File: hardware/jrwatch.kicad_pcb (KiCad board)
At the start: 4 copper layers, 36 x 36 mm, 47 parts, among them J1 TYPE-C-31-M-12, J2 FH12A-10S-0.5SH, J3 SM02B-SRSS-TB, J4 TC2030-IDC-NL, SW1 PWR/SHIP, SW2 USER, U1 MDBT50Q-1MV2, U2 nPM1300-QEAA-R7, U3 BMI270, U4 USBLC6-2SC6, Y1 32.768kHz

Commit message: Critical-net routing clean: USB pair, buck loops, crystal, VBUS entry, pours
Hand-constrained routes verified to zero DRC conflicts before autorouting.
Debug trail: QFN top row numbers right-to-left after flip, rot-90 passives
put pad1 south, USB-C A/B pads land mirrored — every hardcoded coordinate
re-derived from measured pad positions. One deliberate F.Cu crossover for
the interleaved USB pair; long USB run rides the empty top layer. USB skew
7.0mm = 46ps, 0.06% of a FS bit — documented, no serpentine.
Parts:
- moved R1 23.5 mm to (110.0, 101.5)
- moved R2 22.4 mm to (110.0, 103.2)
- moved C15 13.7 mm to (93.2, 98.6), turned to 180 degrees
- moved C4 11.3 mm to (84.7, 107.0)
- turned C16 to -90 degrees
- turned C17 to -90 degrees
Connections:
- U4 pad 1: USB_DP_CONN -> USB_DM_CONN
- U4 pad 3: USB_DM_CONN -> USB_DP_CONN
- U4 pad 4: USB_DM -> USB_DP
- U4 pad 6: USB_DP -> USB_DM
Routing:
- net 3V0: track 0.00 -> 19.9 mm, vias 0 -> 6
- net USB_DP_CONN: track 0.00 -> 17.1 mm
- net USB_DM_CONN: track 0.00 -> 16.8 mm, vias 0 -> 2
- net USB_DP: track 0.00 -> 16.1 mm, vias 0 -> 2
- net USB_DM: track 0.00 -> 13.0 mm, vias 0 -> 2
- net GND: track 0.00 -> 7.51 mm, vias 0 -> 8
- net N$3: track 0.00 -> 6.16 mm
- net 1V8_AUX: track 0.00 -> 5.20 mm
- net XL1: track 0.00 -> 5.08 mm
- net XL2: track 0.00 -> 4.57 mm
- net N$1: track 0.00 -> 4.57 mm
- net VBUS_USB: track 0.00 -> 1.72 mm, vias 0 -> 1
- added copper zone on In1.Cu, net 3V0
- added copper zone on B.Cu, net GND
- added copper zone on F.Cu, net GND
- added copper zone on In2.Cu, net GND
- added copper zone on In1.Cu, net VBAT
- added copper zone on In1.Cu, net VBUS_USB
- added copper zone on In1.Cu, net VSYS

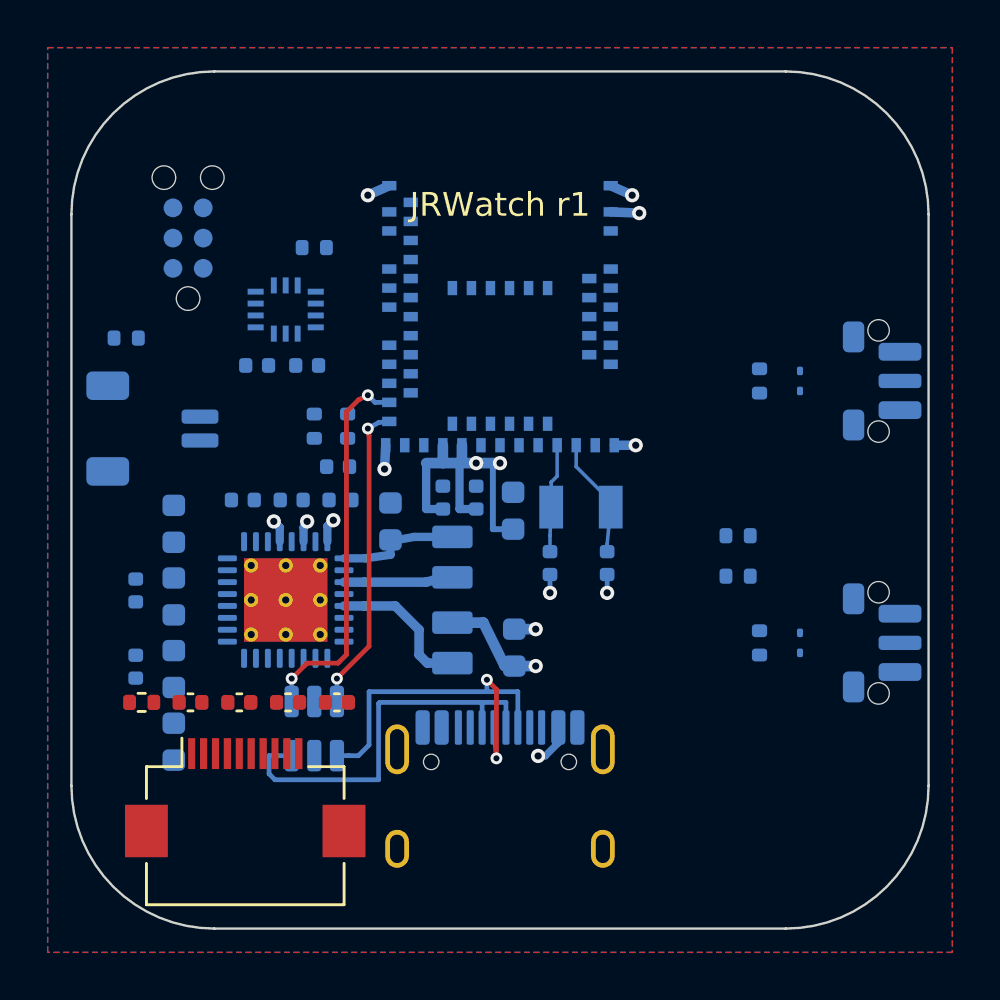
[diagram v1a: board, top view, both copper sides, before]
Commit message: Autoroute round 3: planes locked, edge ring; zero conflicts, links pending
Freerouting cannot stitch into power planes, so plane-net pads and a few
congested signals remain open (completion router next). Edge keep-out ring
added structurally; In1/In2 exported as power layers.
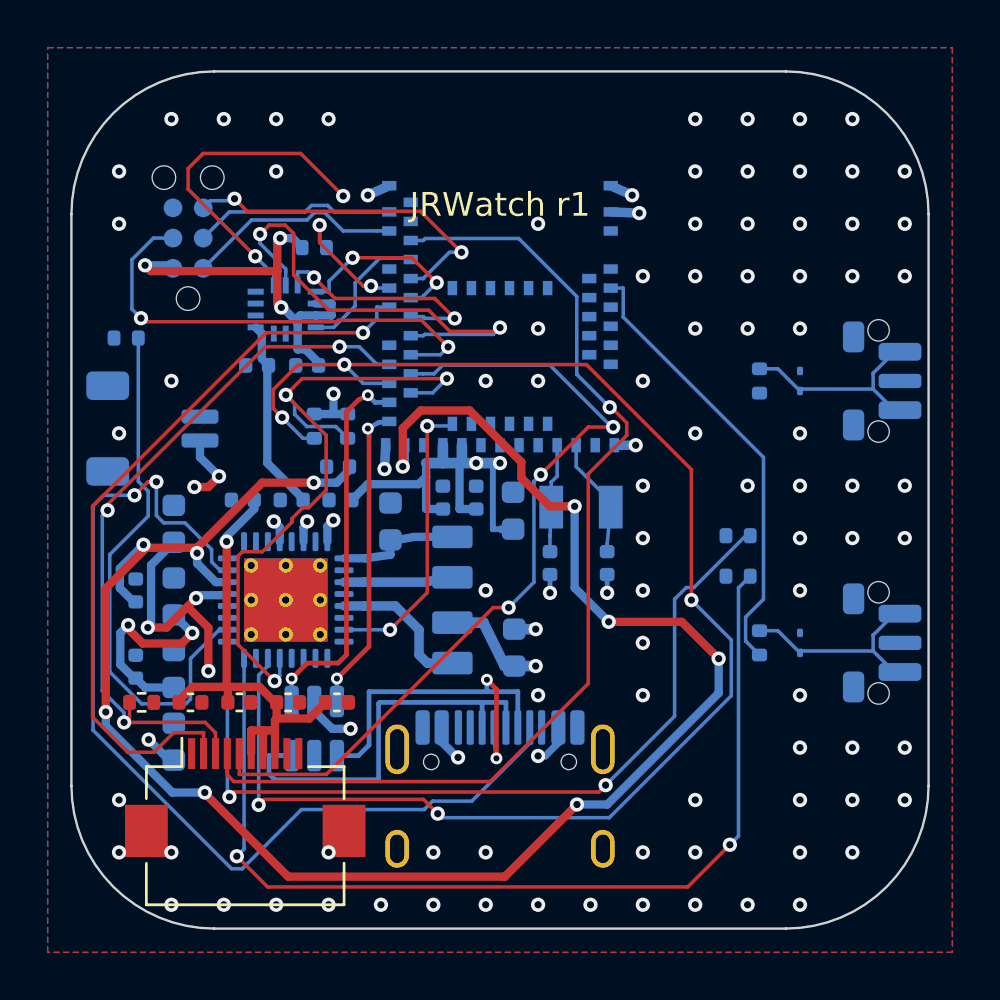
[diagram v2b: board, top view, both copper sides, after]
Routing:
- net VBUS_OUT: track 0.00 -> 79.6 mm, vias 0 -> 10
- net I2C_SCL: track 0.00 -> 64.0 mm, vias 0 -> 5
- net EXTCOMIN: track 0.00 -> 43.7 mm, vias 0 -> 1
- net N$4: track 0.00 -> 42.0 mm, vias 0 -> 2
- net CC1: track 0.00 -> 41.8 mm, vias 0 -> 2
- net N$2: track 0.00 -> 35.9 mm, vias 0 -> 2
- net DISP_ON: track 0.00 -> 34.8 mm, vias 0 -> 3
- net DISP_MOSI: track 0.00 -> 31.6 mm, vias 0 -> 1
- net DISP_CS: track 0.00 -> 30.2 mm, vias 0 -> 3
- net I2C_SDA: track 0.00 -> 29.0 mm, vias 0 -> 3
- net 3V0: track 19.9 -> 46.9 mm, vias 6 -> 10
- net NTC: track 0.00 -> 22.6 mm
- net VDD_DISP: track 0.00 -> 21.2 mm, vias 0 -> 1
- net IMU_CS: track 0.00 -> 21.1 mm, vias 0 -> 4
- net nRESET: track 0.00 -> 19.9 mm, vias 0 -> 2
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
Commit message: Board frozen: zero DRC violations; 7 links documented for interactive completion
Final state: all critical nets hand-routed and locked, autoroute imported
clean, pocket surgery connects LSIN/VOUT2/VDD_DISP/VDD_IMU via on-column
0.48/0.2 vias, hole-to-hole trio fixed by drill shrink, SDA re-routed
around the new vias. Remaining: 7 U2-adjacent links + GND island stitches,
each with exact endpoints and a suggested fix in the review checklist —
left open deliberately rather than routed with violations.
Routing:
- net VDD_DISP: track 21.2 -> 23.9 mm
- net VDD_IMU: track 8.12 -> 10.2 mm
- net 3V0: track 46.9 -> 46.4 mm
- net GND: vias 93 -> 91
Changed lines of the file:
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@@
 		(at 93.2616 93.5625)
 		(size 0.6)
-		(drill 0.3)
+		(drill 0.2)
 		(layers "F.Cu" "B.Cu")
 		(net "DISP_CS")
@@
 	)
 	(segment
+		(start 91.02 100.52)
+		(end 89.9 100.52)
+		(width 0.15)
+		(layer "B.Cu")
+		(net "VDD_DISP")
+	)
+	(segment
 		(start 88.517 101.5344)
 		(end 88.517 101.746)
@@
 		(net "VDD_DISP")
 	)
+	(segment
+		(start 91.25 101.75)
+		(end 91.25 100.75)
+		(width 0.15)
+		(layer "B.Cu")
+		(net "VDD_DISP")
+	)
+	(segment
+		(start 91.25 100.75)
+		(end 91.02 100.52)
+		(width 0.15)
+		(layer "B.Cu")
+		(net "VDD_DISP")
+	)
+	(segment
+		(start 89.9 100.52)
+		(end 89.68 100.37)
+		(width 0.15)
+		(layer "B.Cu")
+		(net "VDD_DISP")
+	)
 	(via
 		(at 99.4 95)
@@
 	)
 	(via
-		(at 117 86.2)
-		(size 0.6)
-		(drill 0.3)
-		(layers "F.Cu" "B.Cu")
-		(net "GND")
-	)
-	(via
 		(at 88.4 117)
 		(size 0.6)
@@
 		(at 95.15 98.7)
 		(size 0.6)
-		(drill 0.3)
+		(drill 0.2)
 		(layers "F.Cu" "B.Cu")
 		(locked yes)
@@
 	)
 	(via
-		(at 86.2 117)
-		(size 0.6)
-		(drill 0.3)
-		(layers "F.Cu" "B.Cu")
-		(net "GND")
-	)
-	(via
 		(at 108.2 84)
 		(size 0.6)
@@
 	)
 	(via
-		(at 91.9 100.9)
-		(size 0.6)
-		(drill 0.3)
+		(at 92.75 100.97)
+		(size 0.48)
+		(drill 0.2)
 		(layers "F.Cu" "B.Cu")
-		(locked yes)
 		(net "3V0")
 	)
 	(via
-		(at 99 98.45)
-		(size 0.6)
-		(drill 0.3)
+		(at 90.75 100.97)
+		(size 0.48)
+		(drill 0.2)
 		(layers "F.Cu" "B.Cu")
-		(locked yes)
 		(net "3V0")
 	)
 	(via
-		(at 85.0924 90.142)
+		(at 99 98.45)
 		(size 0.6)
 		(drill 0.3)
 		(layers "F.Cu" "B.Cu")
+		(locked yes)
 		(net "3V0")
 	)
 	(via
-		(at 90.5 100.9)
-		(size 0.6)
-		(drill 0.3)
+		(at 91.75 100.97)
+		(size 0.48)
+		(drill 0.2)
 		(layers "F.Cu" "B.Cu")
-		(locked yes)
 		(net "3V0")
 	)
 	(via
-		(at 93 100.85)
+		(at 85.0924 90.142)
 		(size 0.6)
 		(drill 0.3)
 		(layers "F.Cu" "B.Cu")
-		(locked yes)
 		(net "3V0")
 	)
@@
 	)
 	(segment
-		(start 92.75 101.75)
-		(end 92.75 101.1)
-		(width 0.35)
-		(locked yes)
-		(layer "B.Cu")
-		(net "3V0")
-	)
-	(segment
 		(start 91.2926 89.0026)
 		(end 90.7663 89.0026)
@@
 	)
 	(segment
+		(start 90.75 101.75)
+		(end 90.75 100.97)
+		(width 0.25)
+		(layer "B.Cu")
+		(net "3V0")
+	)
+	(segment
 		(start 98 105.15)
 		(end 99.3 105.15)
@@
 	(segment
 		(start 91.75 101.75)
-		(end 91.75 101.15)
-		(width 0.35)
-		(locked yes)
+		(end 91.75 100.97)
+		(width 0.25)
 		(layer "B.Cu")
 		(net "3V0")
@@
 	)
 	(segment
-		(start 91.75 101.15)
-		(end 91.9 100.9)
-		(width 0.35)
-		(locked yes)
+		(start 92.75 101.75)
+		(end 92.75 100.97)
+		(width 0.25)
 		(layer "B.Cu")
 		(net "3V0")
@@
 	)
 	(segment
-		(start 90.75 101.75)
-		(end 90.75 101.15)
-		(width 0.35)
-		(locked yes)
-		(layer "B.Cu")
-		(net "3V0")
-	)
-	(segment
-		(start 92.75 101.1)
-		(end 93 100.85)
-		(width 0.35)
-		(locked yes)
-		(layer "B.Cu")
-		(net "3V0")
-	)
-	(segment
 		(start 85.0924 90.142)
 		(end 86.137 90.142)
@@
 	)
 	(segment
-		(start 90.75 101.15)
-		(end 90.5 100.9)
-		(width 0.35)
-		(locked yes)
-		(layer "B.Cu")
-		(net "3V0")
-	)
-	(segment
 		(start 98.3 100.38)
 		(end 98.72 100.38)
@@
 		(at 95.9152 98.5964)
 		(size 0.6)
-		(drill 0.3)
+		(drill 0.2)
 		(layers "F.Cu" "B.Cu")
 		(net "VBUS_OUT")
@@
 	)
 	(segment
-		(start 90.775 110.739)
-		(end 91.2485 110.739)
-		(width 0.2)
-		(layer "B.Cu")
-		(net "USB_DP_CONN")
-	)
-	(segment
 		(start 90.55 111.75)
 		(end 90.3 111.5)
@@
 		(at 91.25 107.5)
 		(size 0.5)
-		(drill 0.25)
+		(drill 0.2)
 		(layers "F.Cu" "B.Cu")
 		(locked yes)
@@
 	)
 	(segment
+		(start 92.25 100)
+		(end 91.9 100)
+		(width 0.15)
+		(layer "B.Cu")
+		(net "VDD_IMU")
+	)
+	(segment
 		(start 91.73 99.9512)
 		(end 91.73 100)
@@
 	)
 	(segment
+		(start 92.25 101.75)
+		(end 92.25 100)
+		(width 0.15)
+		(layer "B.Cu")
+		(net "VDD_IMU")
+	)
+	(segment
 		(start 89.9952 93.0077)
 		(end 89.7375 92.75)
@@
 		(at 93.4633 94.3127)
 		(size 0.6)
-		(drill 0.3)
+		(drill 0.2)
 		(layers "F.Cu" "B.Cu")
 		(net "I2C_SCL")
@@
 	)
 	(segment
-		(start 90.0201 102.1736)
-		(end 91.2599 100.9338)
+		(start 90.75 102)
+		(end 91.26 101.35)
 		(width 0.15)
 		(layer "F.Cu")
@@
 	)
 	(segment
+		(start 90.02 102.17)
+		(end 90.75 102)
+		(width 0.15)
+		(layer "F.Cu")
+		(net "I2C_SDA")
+	)
+	(segment
 		(start 91.2599 100.9338)
 		(end 91.2599 100.7814)
@@
 	)
 	(segment
+		(start 91.26 101.35)
+		(end 91.26 100.93)
+		(width 0.15)
+		(layer "F.Cu")
+		(net "I2C_SDA")
+	)
+	(segment
 		(start 91.7165 100.3248)
 		(end 91.9624 100.3248)
@@
 		(at 90.5333 107.6045)
 		(size 0.6)
-		(drill 0.3)
+		(drill 0.2)
 		(layers "F.Cu" "B.Cu")
 		(net "I2C_SDA")
@@
 		(name "GND_FILL_F")
 		(hatch edge 0.5)
-		(connect_pads
+		(connect_pads yes
 			(clearance 0.2)
 		)
@@
 		(name "GND_FILL_B")
 		(hatch edge 0.5)
-		(connect_pads
+		(connect_pads yes
 			(clearance 0.2)
 		)
@@
 		(hatch edge 0.5)
 		(priority 1)
-		(connect_pads
+		(connect_pads yes
 			(clearance 0.2)
 		)
@@
 		(hatch edge 0.5)
 		(priority 1)
-		(connect_pads
+		(connect_pads yes
 			(clearance 0.2)
 		)
@@
 		(hatch edge 0.5)
 		(priority 1)
-		(connect_pads
+		(connect_pads yes
 			(clearance 0.2)
 		)
@@
 		(hatch edge 0.5)
 		(priority 1)
-		(connect_pads
+		(connect_pads yes
 			(clearance 0.2)
 		)
@@
 		(name "GND_PLANE_IN2")
 		(hatch edge 0.5)
-		(connect_pads
+		(connect_pads yes
 			(clearance 0.2)
 		)

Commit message: Close PMIC power links: VBAT, VSYS x2 via pocket reshuffle, zero DRC
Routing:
- net VSYS: track 10.7 -> 23.4 mm, vias 2 -> 3
- net VBAT: track 4.47 -> 7.20 mm, vias 3 -> 4
- net NTC: track 22.6 -> 23.4 mm
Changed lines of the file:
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@@
+		(net "VBAT")
+	)
+	(via
+		(at 87.2 106.35)
+		(size 0.45)
+		(drill 0.2)
+		(layers "F.Cu" "B.Cu")
 		(net "VBAT")
 	)
@@
 	)
 	(segment
+		(start 87.9 104.95)
+		(end 87.64 105.3)
+		(width 0.15)
+		(layer "B.Cu")
+		(net "VBAT")
+	)
+	(segment
+		(start 87.64 105.3)
+		(end 87.64 106.1)
+		(width 0.15)
+		(layer "B.Cu")
+		(net "VBAT")
+	)
+	(segment
+		(start 87.4 106.35)
+		(end 87.2 106.35)
+		(width 0.15)
+		(layer "B.Cu")
+		(net "VBAT")
+	)
+	(segment
+		(start 87.64 106.1)
+		(end 87.4 106.35)
+		(width 0.15)
+		(layer "B.Cu")
+		(net "VBAT")
+	)
+	(segment
 		(start 85.2418 110.0653)
 		(end 86.1015 110.925)
@@
 		(width 0.35)
 		(layer "B.Cu")
+		(net "VBAT")
+	)
+	(segment
+		(start 88.55 104.95)
+		(end 87.9 104.95)
+		(width 0.25)
+		(layer "B.Cu")
+		(net "VBAT")
+	)
+	(segment
+		(start 87.2 106.35)
+		(end 86.9 106.35)
+		(width 0.35)
+		(layer "In1.Cu")
 		(net "VBAT")
 	)
@@
 	(via
 		(at 87.7522 107.1829)
-		(size 0.6)
-		(drill 0.3)
+		(size 0.45)
+		(drill 0.2)
 		(layers "F.Cu" "B.Cu")
 		(net "VBUS_USB")
@@
 		(net "VSYS")
 	)
+	(via
+		(at 96.11 104.03)
+		(size 0.45)
+		(drill 0.2)
+		(layers "F.Cu" "B.Cu")
+		(net "VSYS")
+	)
+	(segment
+		(start 93.85 103.95)
+		(end 96.05 103.95)
+		(width 0.25)
+		(layer "B.Cu")
+		(net "VSYS")
+	)
 	(segment
 		(start 87.0613 105.5863)
@@
 	)
 	(segment
+		(start 96.05 103.95)
+		(end 96.11 104.03)
+		(width 0.25)
+		(layer "B.Cu")
+		(net "VSYS")
+	)
+	(segment
 		(start 84.0524 106.9108)
 		(end 84.0524 105.5844)
@@
 	)
 	(segment
+		(start 88.55 104.45)
+		(end 87.7 104.45)
+		(width 0.25)
+		(layer "B.Cu")
+		(net "VSYS")
+	)
+	(segment
+		(start 87.7 104.45)
+		(end 87.45 104.9)
+		(width 0.25)
+		(layer "B.Cu")
+		(net "VSYS")
+	)
+	(segment
 		(start 87.0761 105.5863)
 		(end 87.0761 105.5864)
@@
 	)
 	(segment
+		(start 87.45 104.9)
+		(end 87.076 105.586)
+		(width 0.25)
+		(layer "B.Cu")
+		(net "VSYS")
+	)
+	(segment
 		(start 84.6216 107.48)
 		(end 84.0524 106.9108)
@@
 	)
 	(segment
+		(start 96.11 104.03)
+		(end 94 103.82)
+		(width 0.35)
+		(layer "In1.Cu")
+		(net "VSYS")
+	)
+	(segment
+		(start 93.6 104.925)
+		(end 89.2 104.925)
+		(width 0.35)
+		(layer "In1.Cu")
+		(net "VSYS")
+	)
+	(segment
+		(start 89.2 104.925)
+		(end 88.85 105.269)
+		(width 0.35)
+		(layer "In1.Cu")
+		(net "VSYS")
+	)
+	(segment
 		(start 88.85 105.2694)
 		(end 87.3931 105.2694)
+		(width 0.35)
+		(layer "In1.Cu")
+		(net "VSYS")
+	)
+	(segment
+		(start 94 103.82)
+		(end 93.6 104.925)
 		(width 0.35)
 		(layer "In1.Cu")
@@
 	)
 	(segment
-		(start 87.0011 108.3588)
-		(end 87.0011 106.6612)
+		(start 88.212 105.45)
+		(end 87.93 105.73)
 		(width 0.15)
 		(layer "B.Cu")
@@
 	)
 	(segment
-		(start 87.0011 106.6612)
-		(end 88.2123 105.45)
+		(start 86.9 108.56)
+		(end 86.802 108.558)
+		(width 0.15)
+		(layer "B.Cu")
+		(net "NTC")
+	)
+	(segment
+		(start 88.24 106.86)
+		(end 88.24 108.1)
 		(width 0.15)
 		(layer "B.Cu")
@@
 	)
 	(segment
+		(start 87.93 105.73)
+		(end 87.93 106.55)
+		(width 0.15)
+		(layer "B.Cu")
+		(net "NTC")
+	)
+	(segment
 		(start 88.2123 105.45)
 		(end 88.55 105.45)
@@
 	)
 	(segment
-		(start 86.8015 108.5584)
-		(end 87.0011 108.3588)
+		(start 87.93 106.55)
+		(end 88.24 106.86)
 		(width 0.15)
 		(layer "B.Cu")
@@
 		(width 0.15)
 		(layer "B.Cu")
+		(net "NTC")
+	)
+	(segment
+		(start 88.24 108.1)
+		(end 86.9 108.56)
+		(width 0.15)
+		(layer "B.Cu")

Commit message: Ground island stitching: 13 of 16 islands via-stitched to In2 plane, zero DRC
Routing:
- net GND: vias 91 -> 104
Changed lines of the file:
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@@
+	)
+	(via
+		(at 85.5977 106.801042)
+		(size 0.45)
+		(drill 0.2)
+		(layers "F.Cu" "B.Cu")
+		(net "GND")
 	)
 	(via
@@
 	)
 	(via
+		(at 99 99.42)
+		(size 0.45)
+		(drill 0.2)
+		(layers "F.Cu" "B.Cu")
+		(net "GND")
+	)
+	(via
 		(at 105.7 97.7)
 		(size 0.6)
@@
 	)
 	(via
+		(at 86.3 103.275)
+		(size 0.45)
+		(drill 0.2)
+		(layers "F.Cu" "B.Cu")
+		(net "GND")
+	)
+	(via
 		(at 99.4 103.8)
 		(size 0.6)
@@
 	)
 	(via
+		(at 92.2 109.9375)
+		(size 0.45)
+		(drill 0.2)
+		(layers "F.Cu" "B.Cu")
+		(net "GND")
+	)
+	(via
 		(at 108.2 97.2)
 		(size 0.6)
@@
 	)
 	(via
+		(at 91.840951 95.366267)
+		(size 0.45)
+		(drill 0.2)
+		(layers "F.Cu" "B.Cu")
+		(net "GND")
+	)
+	(via
 		(at 106 90.6)
 		(size 0.6)
@@
 	)
 	(via
+		(at 109.49 103.2)
+		(size 0.45)
+		(drill 0.2)
+		(layers "F.Cu" "B.Cu")
+		(net "GND")
+	)
+	(via
 		(at 114.8 86.2)
 		(size 0.6)
@@
 	)
 	(via
+		(at 86.3 106.825)
+		(size 0.45)
+		(drill 0.2)
+		(layers "F.Cu" "B.Cu")
+		(net "GND")
+	)
+	(via
 		(at 114.8 99.4)
 		(size 0.6)
@@
 	)
 	(via
+		(at 116.2 106)
+		(size 0.45)
+		(drill 0.2)
+		(layers "F.Cu" "B.Cu")
+		(net "GND")
+	)
+	(via
 		(at 110.4 92.8)
 		(size 0.6)
@@
 	)
 	(via
+		(at 100.55 99.675)
+		(size 0.45)
+		(drill 0.2)
+		(layers "F.Cu" "B.Cu")
+		(net "GND")
+	)
+	(via
 		(at 114.8 110.4)
 		(size 0.6)
@@
 	)
 	(via
+		(at 116.2 95)
+		(size 0.45)
+		(drill 0.2)
+		(layers "F.Cu" "B.Cu")
+		(net "GND")
+	)
+	(via
 		(at 101.6 108.2)
 		(size 0.6)
@@
 	)
 	(via
+		(at 84.7 103.32)
+		(size 0.45)
+		(drill 0.2)
+		(layers "F.Cu" "B.Cu")
+		(net "GND")
+	)
+	(via
 		(at 101.6 95)
 		(size 0.6)
@@
 	)
 	(via
+		(at 95.4 100.125)
+		(size 0.45)
+		(drill 0.2)
+		(layers "F.Cu" "B.Cu")
+		(net "GND")
+	)
+	(via
 		(at 110.4 99.4)
 		(size 0.6)
@@
 		(net "GND")
 	)
+	(via
+		(at 97.6 99.42)
+		(size 0.45)
+		(drill 0.2)
+		(layers "F.Cu" "B.Cu")
+		(net "GND")
+	)
